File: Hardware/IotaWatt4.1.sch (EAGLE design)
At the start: 57 parts, among them J2 STEREO_JACK_BOT, J3 STEREO_JACK_BOT, J4 STEREO_JACK_BOT, J5 STEREO_JACK_BOT, J6 STEREO_JACK_BOT

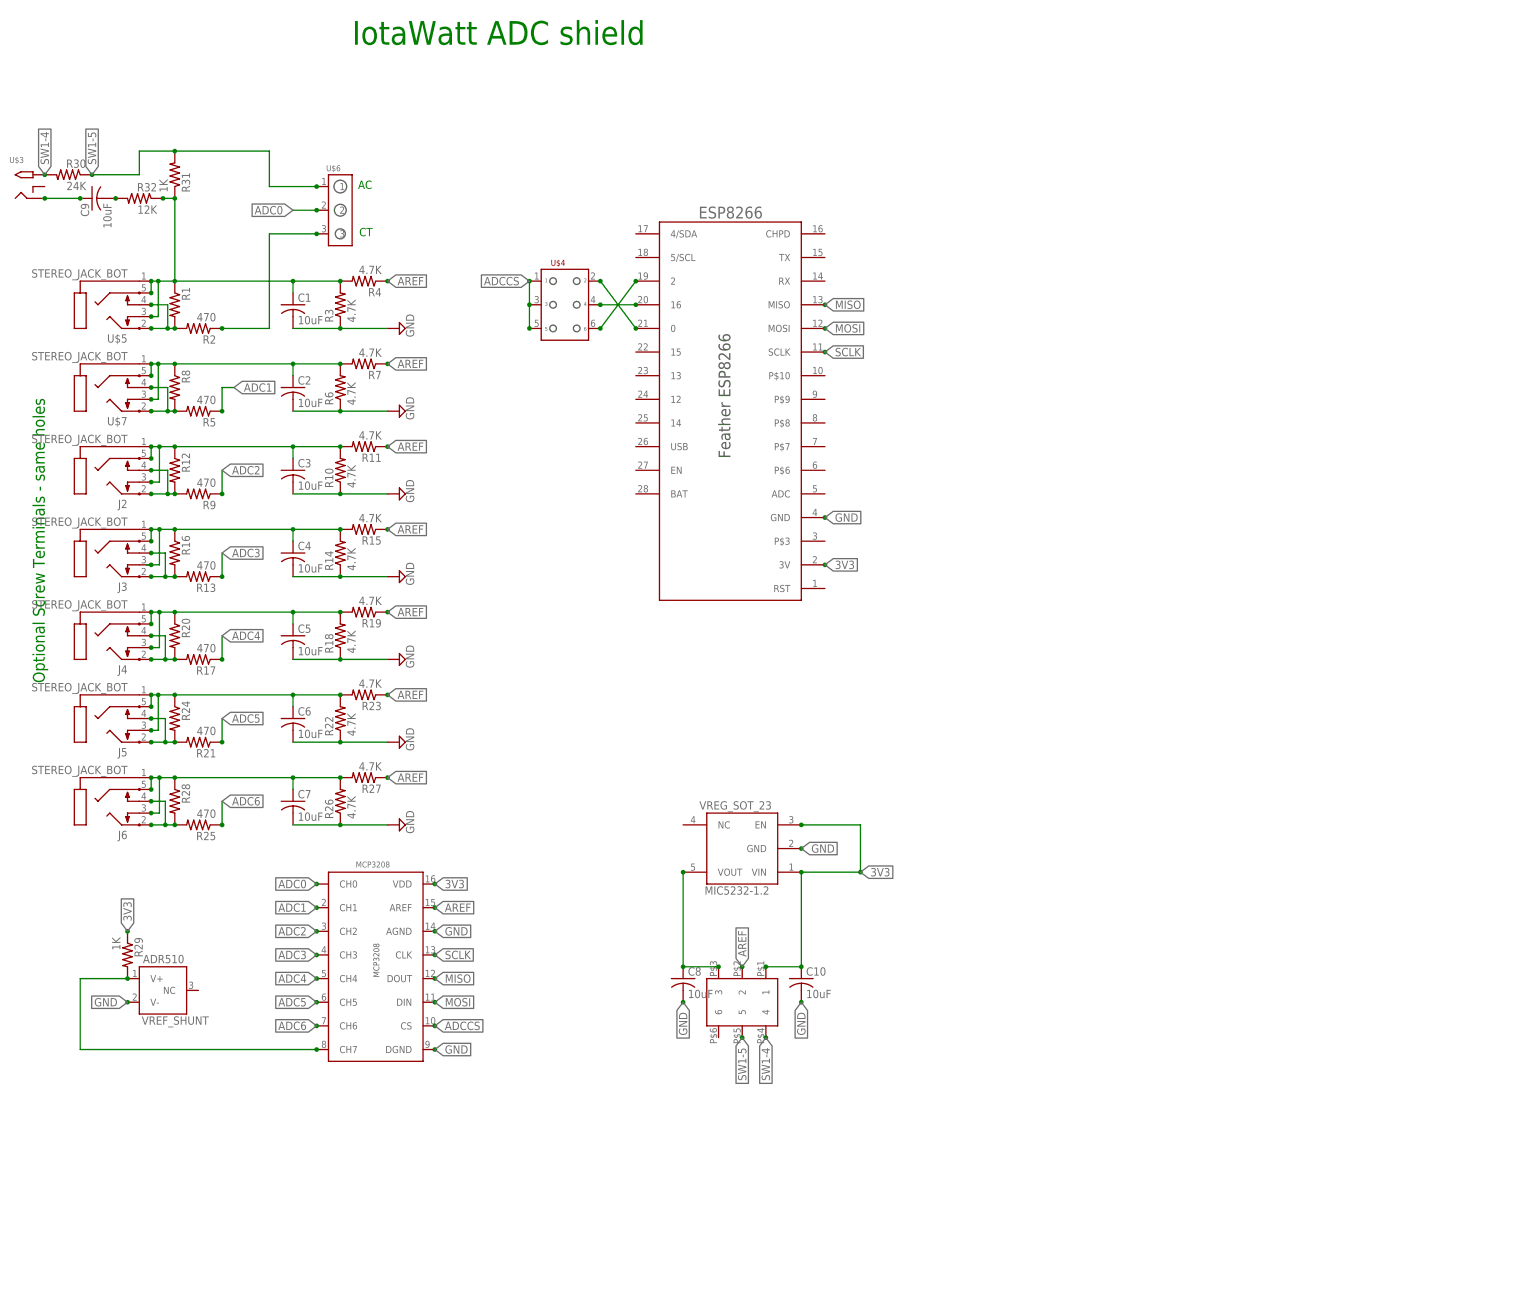
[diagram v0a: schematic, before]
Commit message: Add 4.1 schematic
Add 4.1 schematic.
Remove old hardware versions.
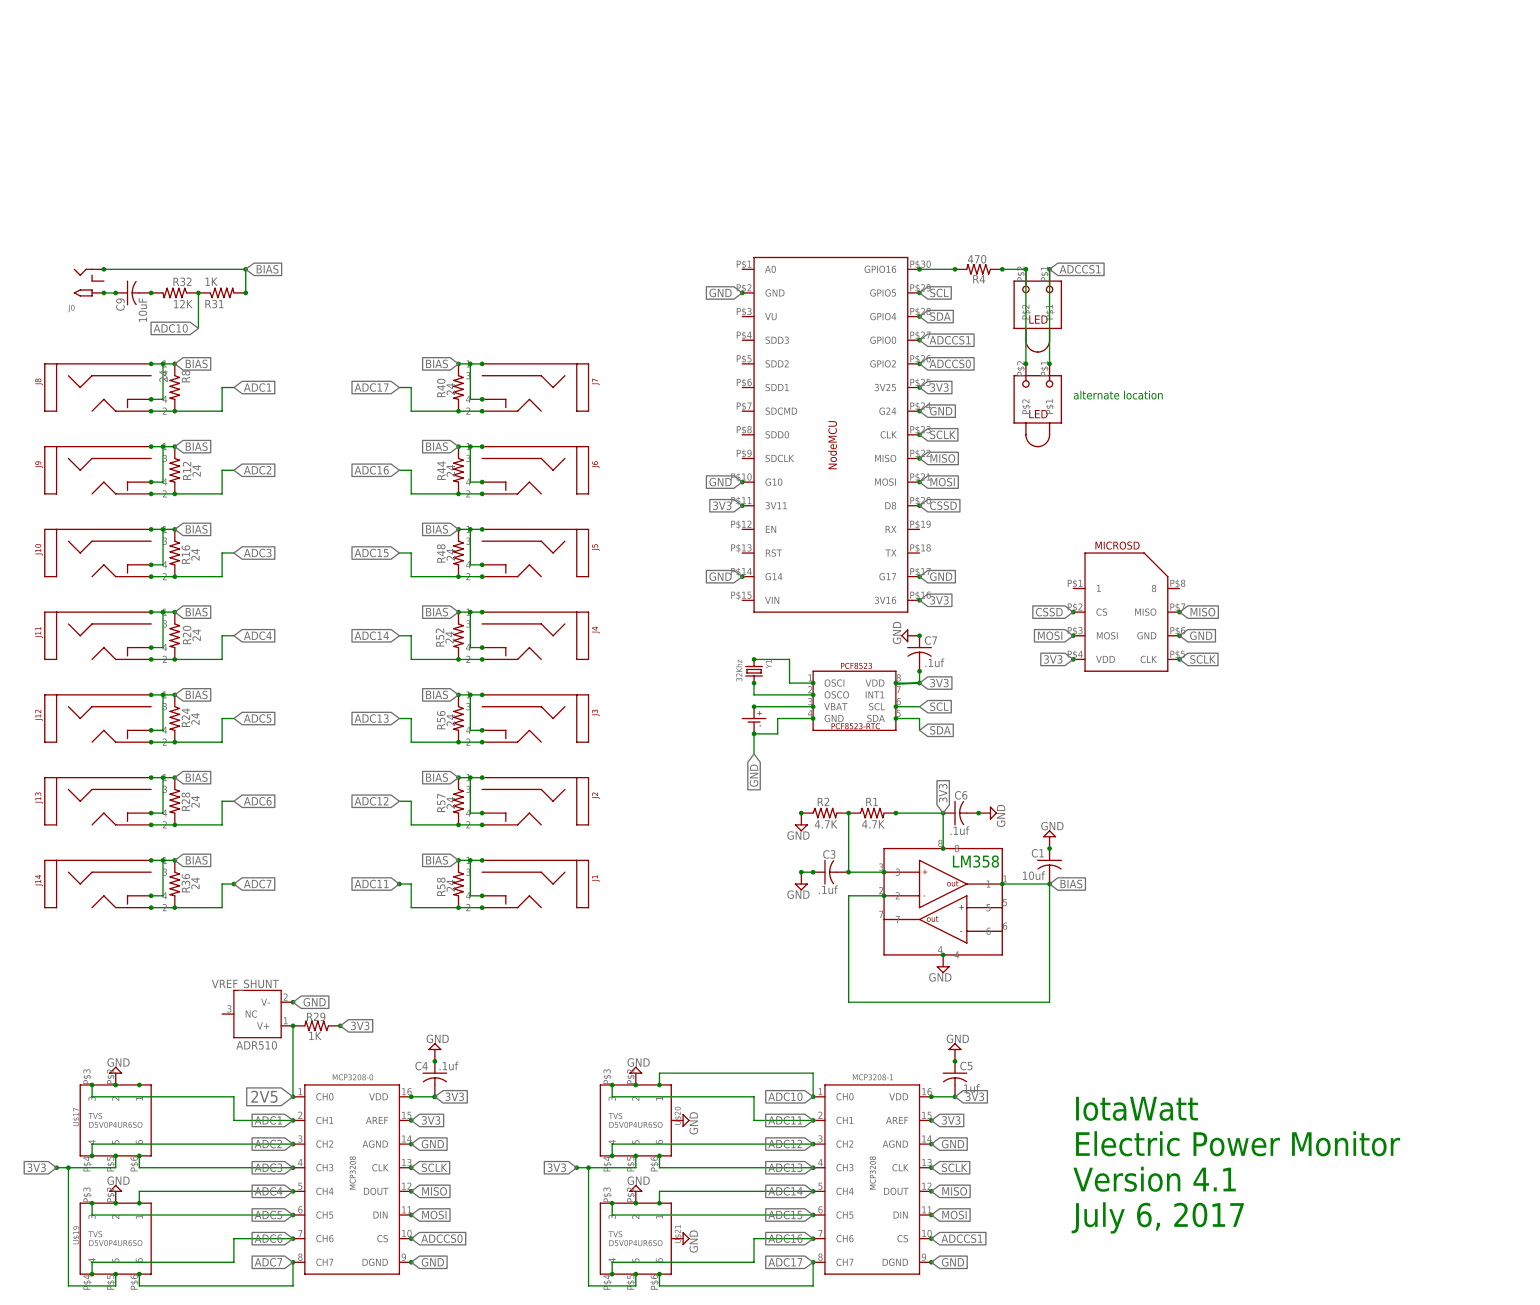
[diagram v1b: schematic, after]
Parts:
- removed C10, C2, C8: 10uF, adafruit:C-USC0805
- removed MCP3208: MCP3208, IotaWatt_parts:MCP3208
- removed MIC5232-1.2: VREG_SOT_23, IotaWatt_parts:VREG_SOT_23
- removed R10, R11, R14, R15, R18, R19, R22, R23, R26, R27, R3, R6, R7: 4.7K, adafruit:R-US_R0805
- removed R13, R17, R21, R25, R5, R9: 470, adafruit:R-US_R0805
- removed R30: 24K, adafruit:R-US_R0805
- removed U$1: ESP8266FEATHER, IotaWatt_parts:ESP8266FEATHER
- removed U$3: 2.1MMJACKBOTTHM, IotaWatt_parts:2.1MMJACKBOTTHM
- removed U$4: HEADER_2X3, IotaWatt_parts:HEADER_2X3
- removed U$5, U$7: STEREO_JACK_BOT, IotaWatt_parts:STEREO_JACK_BOT
- removed U$6: HEADER_1X3, IotaWatt_parts:HEADER_1X3
- removed U$8: DPDT_SMT_SW, IotaWatt_parts:DPDT_SMT_SW
- added J0: 2.1MMJACKSMT, IotaWatt_parts:2.1MMJACKSMT
- added J1, J10, J11, J12, J13, J14, J7, J8, J9: STEREO_SMD, IotaWatt_parts:STEREO_SMD
- added MCP3208-0, MCP3208-1: MCP3208, IotaWatt_parts:MCP3208
- added MICROSD: MICROSD_PUSH/PULL, IotaWatt_parts:MICROSD_PUSH/PULL
- added PCF8523: PCF8523_RTC, IotaWatt_parts:PCF8523_RTC
- added R36, R40, R44, R48, R52, R56, R57, R58: 24, adafruit:R-US_R0805
- added U$15, U$23: LED_RT_TRH, IotaWatt_parts:LED_RT_TRH
- added U$16: NODEMCU, IotaWatt_parts:NODEMCU
- added U$17, U$19, U$20, U$21: TVS_4CHAN_ARRAY, IotaWatt_parts:TVS_4CHAN_ARRAY
- added U$18: CR1220SMD, IotaWatt_parts:CR1220SMD
- added U$22: LM358_DUAL_OP-AMP, IotaWatt_parts:LM358_DUAL_OP-AMP
- added Y1: 32Khz, microbuilder:CRYSTAL8X3.8SMT
- C1: value 10uF -> 10uf
- C3: value 10uF -> .1uf
- C4, C5, C6, C7: value 10uF -> .1uf; device adafruit:C-USC0805 -> adafruit:C-USC0402
- J2, J3, J4, J5, J6: value STEREO_JACK_BOT -> STEREO_SMD; device IotaWatt_parts:STEREO_JACK_BOT -> IotaWatt_parts:STEREO_SMD
- R1: value (none) -> 4.7K; device adafruit:R-US_FLIPFLOP7 -> adafruit:R-US_R0805
- R12, R16, R20, R24, R28, R8: value (none) -> 24; device adafruit:R-US_FLIPFLOP7 -> adafruit:R-US_R0805
- R2: value 470 -> 4.7K
- R4: value 4.7K -> 470
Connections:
- removed net ADC0: MCP3208.CH0, U$6.2
- removed net ADCCS: MCP3208.CS, U$4.P$1, U$4.P$3, U$4.P$5
- removed net AREF: MCP3208.AREF, R11.1, R15.1, R19.1, R23.1, R27.1, R4.1, R7.1, U$8.2
- removed net N$1: R2.1, U$6.3
- removed net N$11: R1.2, R2.2, U$5.3, U$5.5
- removed net N$12: C3.1, J2.1, J2.2, J2.4, R10.2, R11.2, R12.1
- removed net N$13: C5.1, J4.1, J4.2, J4.4, R18.2, R19.2, R20.1
- removed net N$14: J5.3, J5.5, R21.2, R24.2
- removed net N$18: J6.3, J6.5, R25.2, R28.2
- removed net N$19: C7.1, J6.1, J6.2, J6.4, R26.2, R27.2, R28.1
- removed net N$20: R5.2, R8.2, U$7.3, U$7.5
- removed net N$21: J3.3, J3.5, R13.2, R16.2
- removed net N$22: C4.1, J3.1, J3.2, J3.4, R14.2, R15.2, R16.1
- removed net N$24: C8.1, MIC5232-1.2.VOUT, U$8.3
- removed net N$26: J4.3, J4.5, R17.2, R20.2
- removed net N$3: U$1.0, U$4.P$2
- removed net N$4: C2.1, R6.2, R7.2, R8.1, U$7.1, U$7.2, U$7.4
- removed net N$5: J2.3, J2.5, R12.2, R9.2
- removed net N$6: U$1.2, U$4.P$6
- removed net N$9: U$1.16, U$4.P$4
- removed net SW1-4: R30.2, U$3.TIP, U$8.4
- removed net SW1-5: R30.1, R31.2, U$6.1, U$8.5
- new net 2V5: ADR510.V+, MCP3208-0.CH0, R29.2
- new net ADC10: MCP3208-1.CH0, R31.1, R32.1, U$20.1
- new net ADC11: J1.2, MCP3208-1.CH1, R58.2, U$20.3
- new net ADC12: J2.2, MCP3208-1.CH2, R57.2, U$20.4
- new net ADC13: J3.2, MCP3208-1.CH3, R56.2, U$20.6
- new net ADC14: J4.2, MCP3208-1.CH4, R52.2, U$21.1
- new net ADC15: J5.2, MCP3208-1.CH5, R48.2, U$21.3
- new net ADC16: J6.2, MCP3208-1.CH6, R44.2, U$21.4
- new net ADC17: J7.2, MCP3208-1.CH7, R40.2, U$21.6
- new net ADCCS0: MCP3208-0.CS, U$16.GPIO2
- new net ADCCS1: MCP3208-1.CS, U$15.P$1, U$16.GPIO0, U$23.P$1
- new net BIAS: C1.2, J0.RING, J1.1, J1.4, J10.1, J10.4, J11.1, J11.4, J12.1, J12.4, J13.1, J13.4, J14.1, J14.4, J2.1, J2.4, J3.1, J3.4, J4.1, J4.4, J5.1, J5.4, J6.1, J6.4, J7.1, J7.4, J8.1, J8.4, J9.1, J9.4, R12.1, R16.1, R20.1, R24.1, R28.1, R31.2, R36.1, R40.1, R44.1, R48.1, R52.1, R56.1, R57.1, R58.1, R8.1, U$22.1, U$22.2
- new net CSSD: MICROSD.CS, U$16.D8
- new net N$10: R4.2, U$16.GPIO16
- new net N$43: PCF8523.VBAT, U$18.P$+
- new net N$44: PCF8523.OSCO, Y1.2
- new net N$45: PCF8523.OSCI, Y1.1
- new net N$8: R4.1, U$15.P$2, U$23.P$2
- new net SCL: PCF8523.SCL, U$16.GPIO5
- new net SDA: PCF8523.SDA, U$16.GPIO4
- net 3V3: now also C4.2, C5.2, C6.1, C7.2, MCP3208-0.AREF, MCP3208-0.VDD, MCP3208-1.AREF, MCP3208-1.VDD, MICROSD.VDD, PCF8523.VDD, R1.2, U$16.3V11, U$16.3V16, U$16.3V25, U$17.5, U$19.5, U$20.5, U$21.5, U$22.8; no longer C10.1, MCP3208.VDD, MIC5232-1.2.EN, MIC5232-1.2.VIN, U$1.3V, U$8.1
- net ADC1: now also J8.2, MCP3208-0.CH1, R8.2, U$17.3; no longer MCP3208.CH1, R5.1
- net ADC2: now also J9.2, MCP3208-0.CH2, R12.2, U$17.4; no longer MCP3208.CH2, R9.1
- net ADC3: now also J10.2, MCP3208-0.CH3, R16.2, U$17.6; no longer MCP3208.CH3, R13.1
- net ADC4: now also J11.2, MCP3208-0.CH4, R20.2, U$19.1; no longer MCP3208.CH4, R17.1
- net ADC5: now also J12.2, MCP3208-0.CH5, R24.2, U$19.3; no longer MCP3208.CH5, R21.1
- net ADC6: now also J13.2, MCP3208-0.CH6, R28.2, U$19.4; no longer MCP3208.CH6, R25.1
- net ADC7: now also J14.2, MCP3208-0.CH7, R36.2, U$19.6; no longer ADR510.V+, MCP3208.CH7, R29.2
- net GND: now also C1.1, C3.1, C4.1, C5.1, C7.1, MCP3208-0.AGND, MCP3208-0.DGND, MCP3208-1.AGND, MCP3208-1.DGND, MICROSD.GND, PCF8523.GND, R2.1, U$16.G10, U$16.G14, U$16.G17, U$16.G24, U$16.GND, U$17.2, U$18.P$-, U$19.2, U$20.2, U$21.2, U$22.4; no longer C1.2, C10.2, C2.2, C3.2, C4.2, C5.2, C7.2, C8.2, MCP3208.AGND, MCP3208.DGND, MIC5232-1.2.GND, R10.1, R14.1, R18.1, R22.1, R26.1, R3.1, R6.1, U$1.GND
- net MISO: now also MCP3208-0.DOUT, MCP3208-1.DOUT, MICROSD.MISO, U$16.MISO; no longer MCP3208.DOUT, U$1.MISO
- net MOSI: now also MCP3208-0.DIN, MCP3208-1.DIN, MICROSD.MOSI, U$16.MOSI; no longer MCP3208.DIN, U$1.MOSI
- net N$16: now also U$17.1; no longer C6.1, J5.1, J5.2, J5.4, R22.2, R23.2, R24.1
- net N$2: now also C3.2, R2.2, U$22.3; no longer C1.1, R3.2, R31.1, R32.1, R4.2, U$5.1, U$5.2, U$5.4
- net N$27: now also J0.TIP; no longer U$3.RING
- net SCLK: now also MCP3208-0.CLK, MCP3208-1.CLK, MICROSD.CLK, U$16.CLK; no longer MCP3208.CLK, U$1.SCLK
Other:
- note added: "IotaWatt Electric Power Monitor Version 4.1 July 6, 2017"
- note added: "LM358"
- note added: "alternate location"
- note removed: "AC"
- note removed: "CT"
- note removed: "IotaWatt ADC shield"
- note removed: "Optional Screw Terminals - same holes"
- moved on the sheet: ADR510, C1, C3, C4, C5, C6, C7, C9, R1, R2, R29, R31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
